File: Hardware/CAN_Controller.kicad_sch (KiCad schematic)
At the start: 21 parts, among them J1 Conn_01x03, J2 Conn_01x08, J3 Conn_01x02, U1 ATtiny814-SS, U2 MCP2515-xSO, U3 MCP2551-I-SN, U4 MCP16331CH, Y1 8 MHz

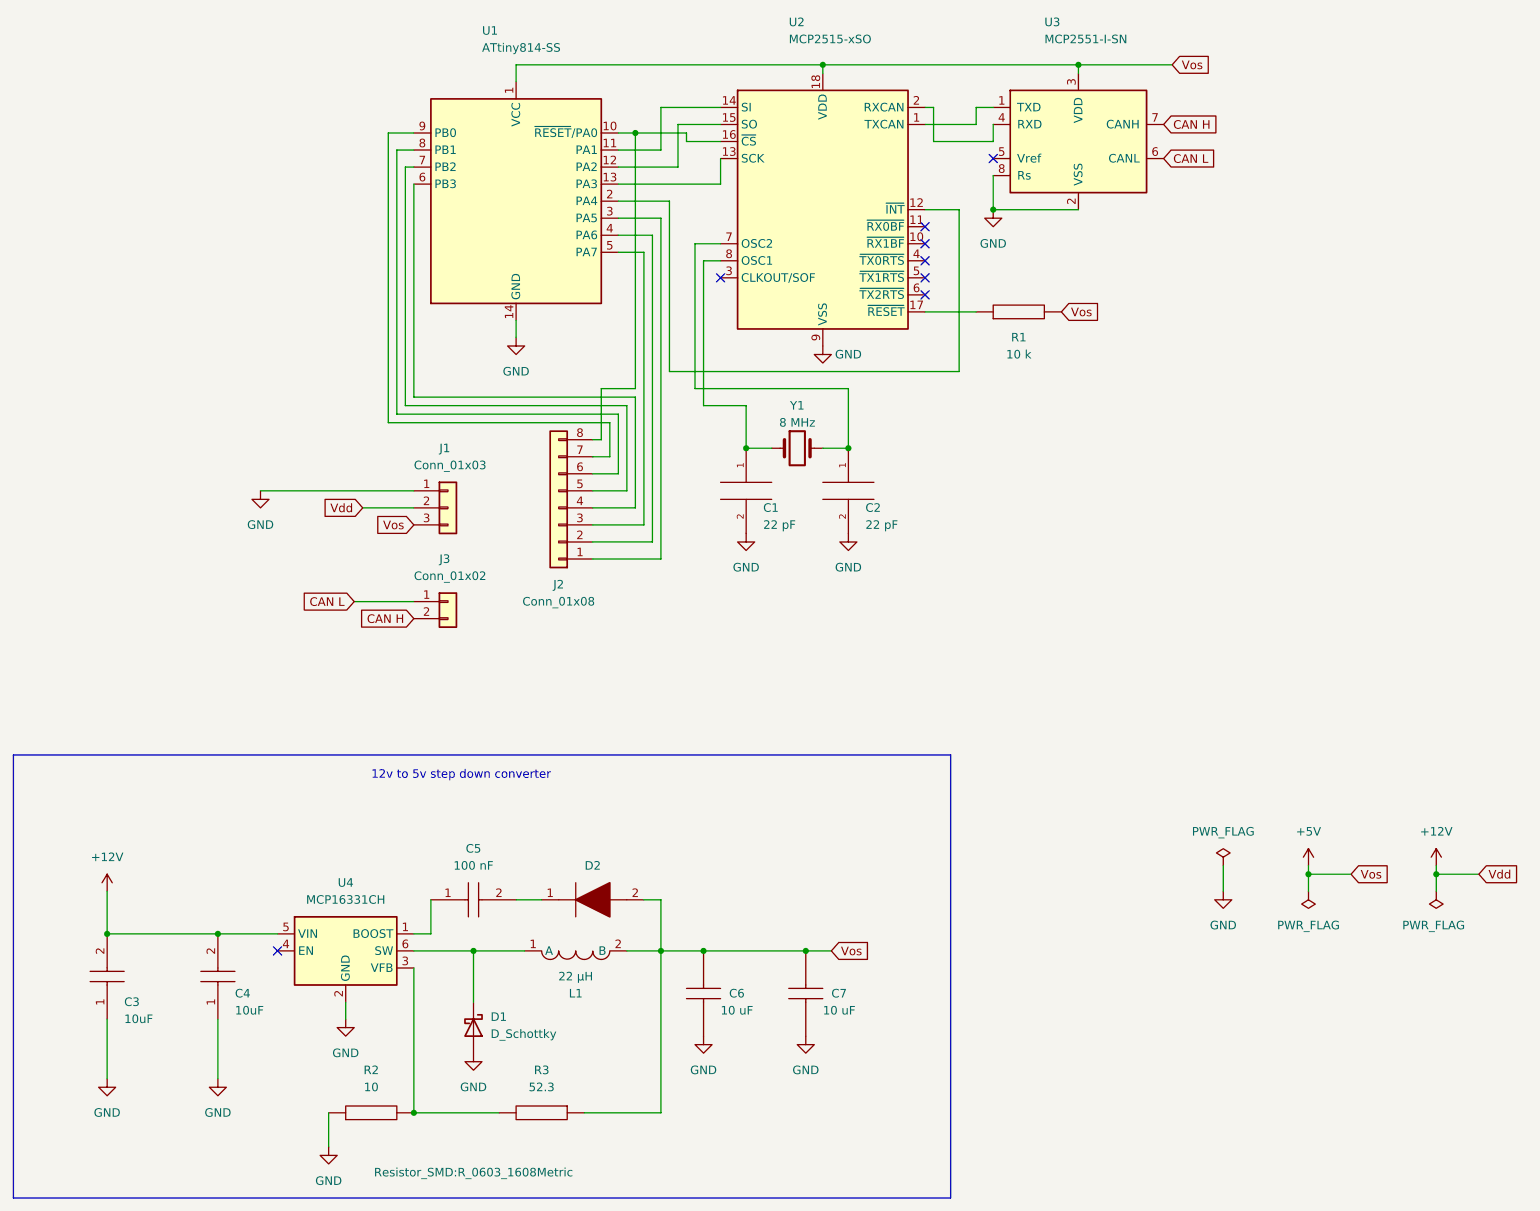
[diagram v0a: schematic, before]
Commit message: rearrainged components to reduce board size and added project footprints
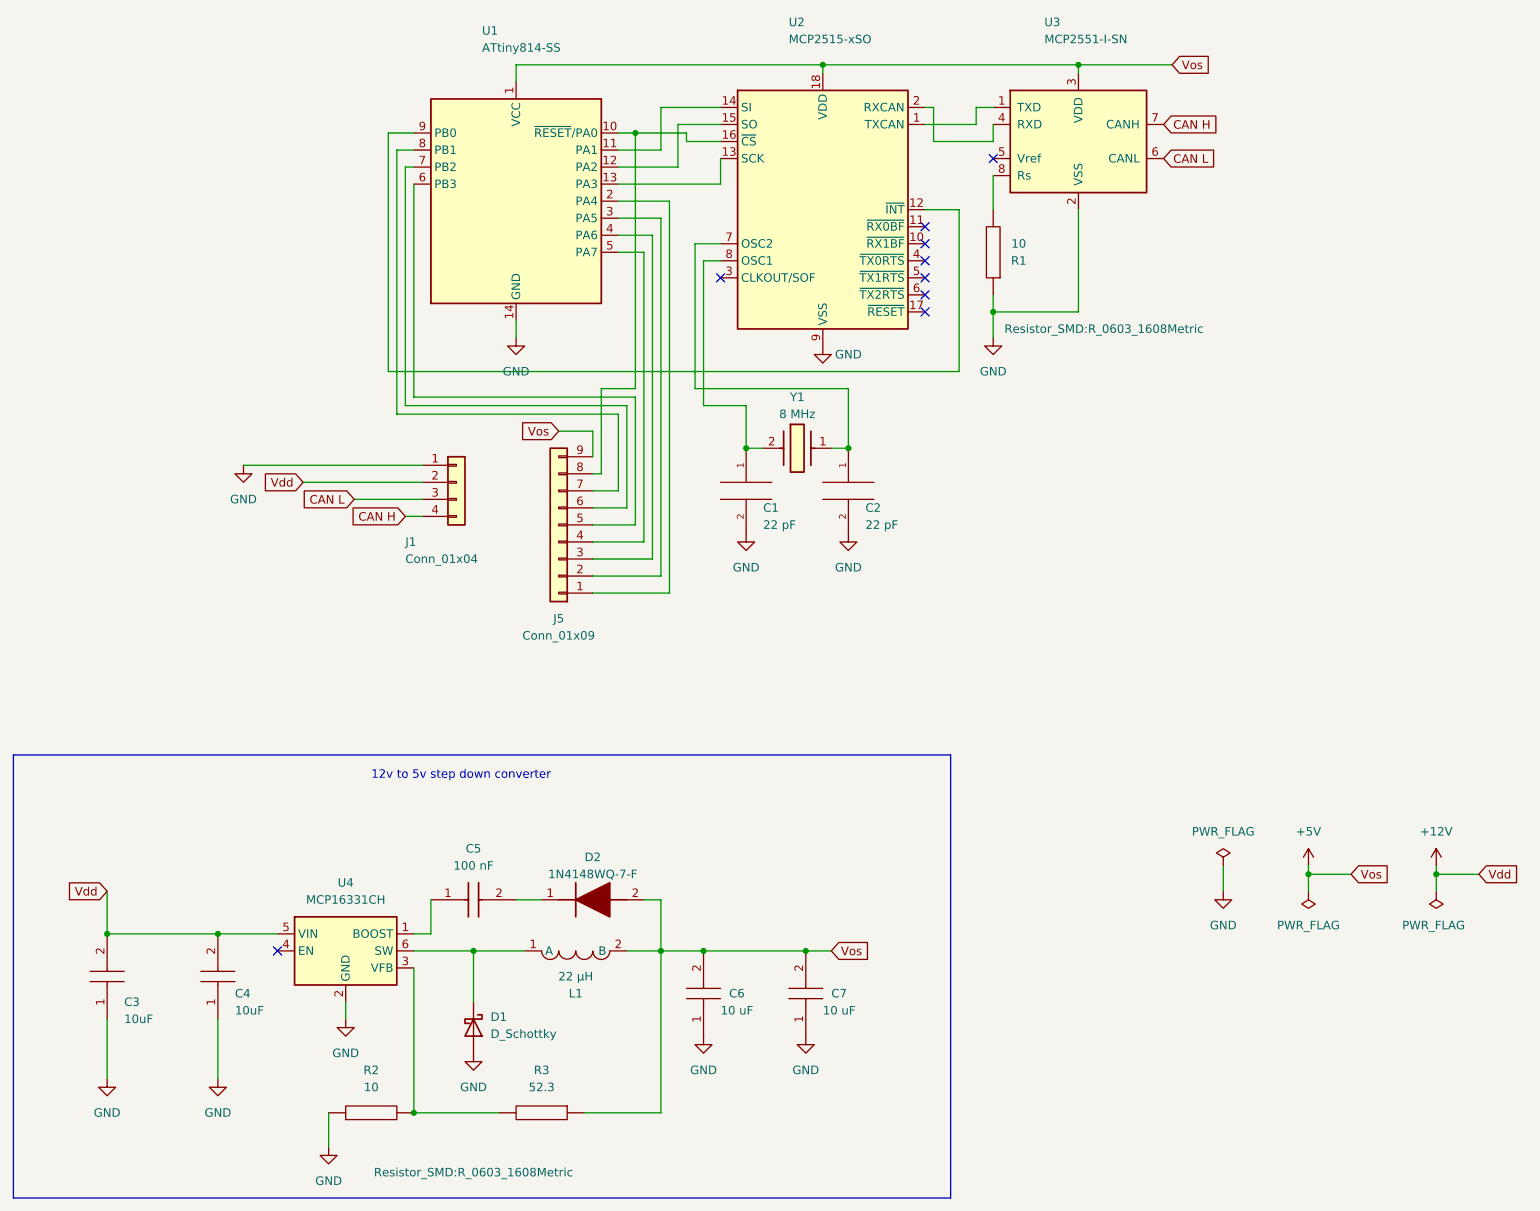
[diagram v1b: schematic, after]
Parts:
- removed D2: 1N4148WQ-7-F, SOD3716X145N, symbol 1N4148_SOD_SMD:1N4148WQ-7-F
- removed J1: Conn_01x03, Connector_PinHeader_2.54mm:PinHeader_1x03_P2.54mm_Vertical, symbol Connector_Generic:Conn_01x03
- removed J2: Conn_01x08, Connector_PinHeader_2.54mm:PinHeader_1x08_P2.54mm_Vertical, symbol Connector_Generic:Conn_01x08
- removed J3: Conn_01x02, Connector_PinHeader_2.54mm:PinHeader_1x02_P2.54mm_Vertical, symbol Connector_Generic:Conn_01x02
- added D2: 1N4148WQ-7-F, SOD3716X145N, symbol 1N4148WQ-7-F:1N4148WQ-7-F
- added J1: Conn_01x04, Connector_PinHeader_2.00mm:PinHeader_1x04_P2.00mm_Vertical, symbol Connector_Generic:Conn_01x04
- added J5: Conn_01x09, Connector_PinHeader_2.00mm:PinHeader_1x09_P2.00mm_Vertical, symbol Connector_Generic:Conn_01x09
- C1, C2: Manufacturer_Part_Number (none) -> C0603C220K3RACAUTO
- C6, C7: footprint C3216_Commercial -> CAPC3216X180N; Height 0.75 -> 1.8
- R1: value 10 k -> 10
- Y1: footprint Crystal:Crystal_SMD_0603-2Pin_6.0x3.5mm -> ECS80830QVSTR; symbol Device:Crystal -> ECS-80-8-30Q-VS-TR:ECS-80-8-30Q-VS-TR; Height (none) -> 1.1; Manufacturer_Name (none) -> ECS; Manufacturer_Part_Number (none) -> ECS-80-8-30Q-VS-TR; Mouser Part Number (none) -> 520-80-8-30Q-VST; Mouser Price/Stock (none) -> https://www.mouser.co.uk/ProductDetail/ECS/ECS-80-8-30Q-VS-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
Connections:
- net +12V: now also J1.2 (Pin_2)
- net +5V: now also D2.2 (A), J5.9 (Pin_9); no longer R1.2
- net CAN H: now also J1.4 (Pin_4)
- net CAN L: now also J1.3 (Pin_3)
- net GND: now also R1.1, J1.1 (Pin_1); no longer U3.8 (Rs)
- net at U2.17 (~{RESET}): no longer R1.1
- net at U1.3 (PA5): now also J5.2 (Pin_2)
- net at U1.4 (PA6): now also J5.3 (Pin_3)
- net at U1.5 (PA7): now also J5.4 (Pin_4)
- net at U1.6 (PB3): now also J5.5 (Pin_5)
- net at U1.7 (PB2): now also J5.6 (Pin_6)
- net at U1.8 (PB1): now also J5.7 (Pin_7)
- net at U1.9 (PB0): now also U2.12 (~{INT})
- net at U1.10 (~{RESET}/PA0), U2.16 (~{CS}): now also J5.8 (Pin_8)
- net at U1.2 (PA4): now also J5.1 (Pin_1); no longer U2.12 (~{INT})
- net at C2.1, U2.7 (OSC2): now also Y1.1 (IN/OUT); no longer Y1.2
- net at C1.1, U2.8 (OSC1): now also Y1.2 (OUT/IN); no longer Y1.1
- net at C5.2: now also D2.1 (K)
- new net: R1.2, U3.8 (Rs)
- no-connect marks 8 -> 9

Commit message: Reduced PCB footprint
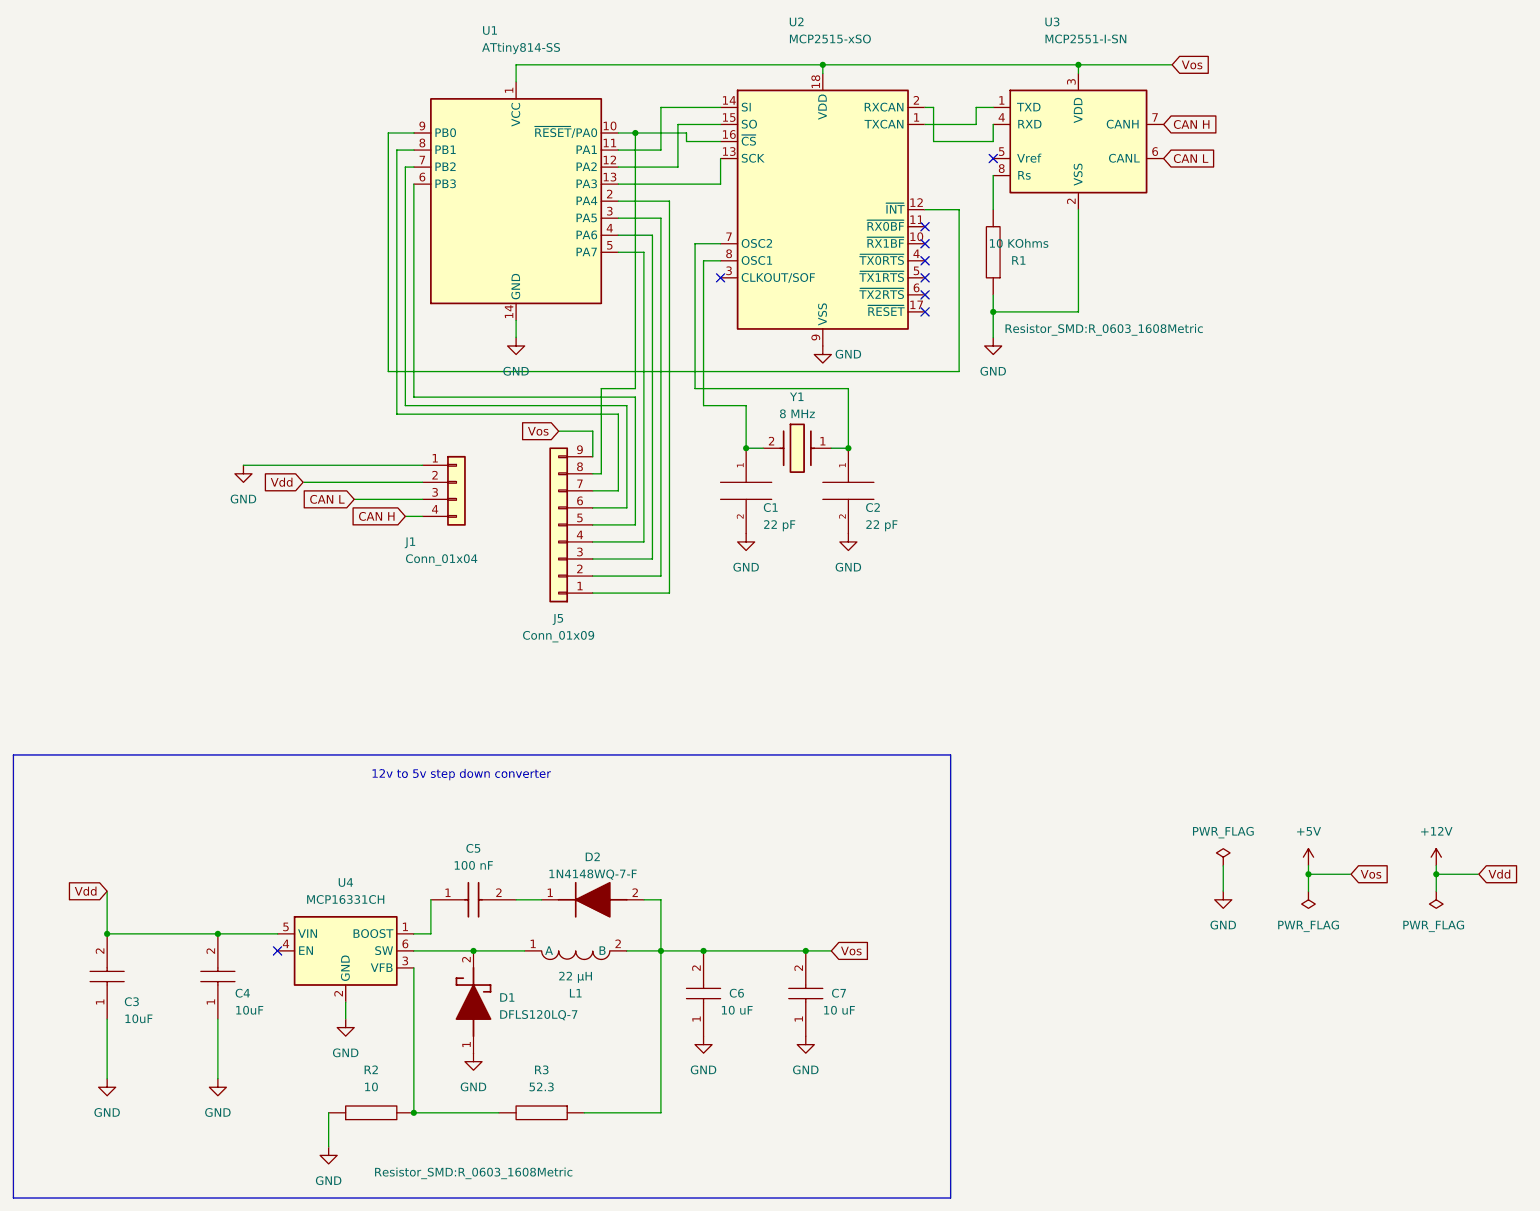
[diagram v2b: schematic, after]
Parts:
- removed D1: D_Schottky, Schottky_Diode:DFLS120L7, symbol Device:D_Schottky
- added D1: DFLS120LQ-7, DFLS120LQ7, symbol DFLS120LQ-7:DFLS120LQ-7
- J1: footprint Connector_PinHeader_2.00mm:PinHeader_1x04_P2.00mm_Vertical -> Connector_PinHeader_2.54mm:PinHeader_1x04_P2.54mm_Vertical
- J5: footprint Connector_PinHeader_2.00mm:PinHeader_1x09_P2.00mm_Vertical -> Connector_PinHeader_2.54mm:PinHeader_1x09_P2.54mm_Vertical
- R1: value 10 -> 10 KOhms
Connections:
- net GND: now also D1.1 (A)
- net at L1.1 (A), U4.6 (SW): now also D1.2 (K)
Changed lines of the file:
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@@
   (junction (at 147.32 24.13) (diameter 0) (color 0 0 0 0)
   )
+  (junction (at 95.25 156.21) (diameter 0) (color 0 0 0 0)
+  )
   (junction (at 219.71 144.78) (diameter 0) (color 0 0 0 0)
-  )
-  (junction (at 95.25 156.21) (diameter 0) (color 0 0 0 0)
   )
   (junction (at 144.78 156.21) (diameter 0) (color 0 0 0 0)
@@
     (stroke (width 0) (type default))
   )
+  (wire (pts (xy 172.72 33.02) (xy 172.72 35.56))
+    (stroke (width 0) (type default))
+  )
+  (wire (pts (xy 185.42 24.13) (xy 199.39 24.13))
+    (stroke (width 0) (type default))
+  )
+  (polyline (pts (xy 26.67 127) (xy 166.37 127))
+    (stroke (width 0) (type default))
+  )
+  (wire (pts (xy 88.9 153.67) (xy 88.9 148.59))
+    (stroke (width 0) (type default))
+  )
+  (polyline (pts (xy 166.37 193.04) (xy 166.37 127))
+    (stroke (width 0) (type default))
+  )
+  (wire (pts (xy 170.18 30.48) (xy 172.72 30.48))
+    (stroke (width 0) (type default))
+  )
+  (wire (pts (xy 107.95 78.74) (xy 113.03 78.74))
+    (stroke (width 0) (type default))
+  )
+  (wire (pts (xy 113.03 97.79) (xy 121.92 97.79))
+    (stroke (width 0) (type default))
+  )
+  (wire (pts (xy 123.19 30.48) (xy 132.08 30.48))
+    (stroke (width 0) (type default))
+  )
+  (wire (pts (xy 123.19 156.21) (xy 123.19 180.34))
+    (stroke (width 0) (type default))
+  )
+  (wire (pts (xy 116.84 49.53) (xy 121.92 49.53))
+    (stroke (width 0) (type default))
+  )
+  (wire (pts (xy 185.42 60.96) (xy 172.72 60.96))
+    (stroke (width 0) (type default))
+  )
+  (wire (pts (xy 86.36 180.34) (xy 86.36 158.75))
+    (stroke (width 0) (type default))
+  )
+  (wire (pts (xy 85.09 39.37) (xy 86.36 39.37))
+    (stroke (width 0) (type default))
+  )
+  (wire (pts (xy 60.96 83.82) (xy 87.63 83.82))
+    (stroke (width 0) (type default))
+  )
+  (wire (pts (xy 82.55 34.29) (xy 86.36 34.29))
+    (stroke (width 0) (type default))
+  )
+  (wire (pts (xy 172.72 60.96) (xy 172.72 64.77))
+    (stroke (width 0) (type default))
+  )
   (wire (pts (xy 95.25 156.21) (xy 102.87 156.21))
     (stroke (width 0) (type default))
   )
-  (wire (pts (xy 172.72 33.02) (xy 172.72 35.56))
-    (stroke (width 0) (type default))
-  )
-  (wire (pts (xy 185.42 24.13) (xy 199.39 24.13))
-    (stroke (width 0) (type default))
-  )
-  (polyline (pts (xy 26.67 127) (xy 166.37 127))
-    (stroke (width 0) (type default))
-  )
-  (wire (pts (xy 88.9 153.67) (xy 88.9 148.59))
-    (stroke (width 0) (type default))
-  )
-  (polyline (pts (xy 166.37 193.04) (xy 166.37 127))
-    (stroke (width 0) (type default))
-  )
-  (wire (pts (xy 170.18 30.48) (xy 172.72 30.48))
-    (stroke (width 0) (type default))
-  )
-  (wire (pts (xy 107.95 78.74) (xy 113.03 78.74))
-    (stroke (width 0) (type default))
-  )
-  (wire (pts (xy 113.03 97.79) (xy 121.92 97.79))
-    (stroke (width 0) (type default))
-  )
-  (wire (pts (xy 123.19 30.48) (xy 132.08 30.48))
-    (stroke (width 0) (type default))
-  )
-  (wire (pts (xy 116.84 49.53) (xy 121.92 49.53))
-    (stroke (width 0) (type default))
-  )
-  (wire (pts (xy 185.42 60.96) (xy 172.72 60.96))
-    (stroke (width 0) (type default))
-  )
-  (wire (pts (xy 86.36 180.34) (xy 86.36 158.75))
-    (stroke (width 0) (type default))
-  )
-  (wire (pts (xy 85.09 39.37) (xy 86.36 39.37))
-    (stroke (width 0) (type default))
-  )
-  (wire (pts (xy 60.96 83.82) (xy 87.63 83.82))
-    (stroke (width 0) (type default))
-  )
-  (wire (pts (xy 82.55 34.29) (xy 86.36 34.29))
-    (stroke (width 0) (type default))
-  )
-  (wire (pts (xy 172.72 60.96) (xy 172.72 64.77))
-    (stroke (width 0) (type default))
-  )
   (wire (pts (xy 83.82 76.2) (xy 116.84 76.2))
     (stroke (width 0) (type default))
@@
     (stroke (width 0) (type default))
   )
-  (wire (pts (xy 123.19 156.21) (xy 123.19 180.34))
-    (stroke (width 0) (type default))
-  )
   (wire (pts (xy 129.54 74.93) (xy 135.89 74.93))
     (stroke (width 0) (type default))
@@
   )
   (wire (pts (xy 119.38 34.29) (xy 127 34.29))
-    (stroke (width 0) (type default))
-  )
-  (wire (pts (xy 95.25 156.21) (xy 95.25 163.83))
     (stroke (width 0) (type default))
   )
@@
       (effects (font (size 1.27 1.27)))
     )
-    (property "Value" "10" (at 176.53 50.8 0)
+    (property "Value" "10 KOhms" (at 176.53 50.8 0)
       (effects (font (size 1.27 1.27)))
     )
@@
     )
   )
+  (symbol (lib_id "DFLS120LQ-7:DFLS120LQ-7") (at 95.25 153.67 270) (unit 1)
+    (in_bom yes) (on_board yes) (dnp no) (fields_autoplaced)
+    (property "Reference" "D1" (at 99.06 163.195 90)
+      (effects (font (size 1.27 1.27)) (justify left))
+    )
+    (property "Value" "DFLS120LQ-7" (at 99.06 165.735 90)
+      (effects (font (size 1.27 1.27)) (justify left))
+    )
+    (property "Footprint" "DFLS120LQ7" (at 1.6 166.37 0)
+      (effects (font (size 1.27 1.27)) (justify left top) hide)
+    )
+    (property "Datasheet" "https://componentsearchengine.com/Datasheets/1/DFLS120LQ-7.pdf" (at -98.4 166.37 0)
+      (effects (font (size 1.27 1.27)) (justify left top) hide)
+    )
+    (property "Height" "" (at -298.4 166.37 0)
+      (effects (font (size 1.27 1.27)) (justify left top) hide)
+    )
+    (property "Mouser Part Number" "621-DFLS120LQ7" (at -398.4 166.37 0)
+      (effects (font (size 1.27 1.27)) (justify left top) hide)
+    )
+    (property "Mouser Price/Stock" "https://www.mouser.com/Search/Refine.aspx?Keyword=621-DFLS120LQ7" (at -498.4 166.37 0)
+      (effects (font (size 1.27 1.27)) (justify left top) hide)
+    )
+    (property "Manufacturer_Name" "Diodes Inc." (at -598.4 166.37 0)
+      (effects (font (size 1.27 1.27)) (justify left top) hide)
+    )
+    (property "Manufacturer_Part_Number" "DFLS120LQ-7" (at -698.4 166.37 0)
+      (effects (font (size 1.27 1.27)) (justify left top) hide)
+    )
+    (pin "1")
+    (pin "2")
+    (instances
+      (project "CAN_Controller"
+        (path "/cd098e14-1fbf-4252-bea9-fb7f332659be"
+          (reference "D1") (unit 1)
+        )
+      )
+    )
+  )
   (symbol (lib_id "power:GND") (at 147.32 66.04 0) (unit 1)
     (in_bom yes) (on_board yes) (dnp no)
@@
       (effects (font (size 1.27 1.27)))
     )
-    (property "Footprint" "Connector_PinHeader_2.00mm:PinHeader_1x09_P2.00mm_Vertical" (at 107.95 92.71 0)
+    (property "Footprint" "Connector_PinHeader_2.54mm:PinHeader_1x09_P2.54mm_Vertical" (at 107.95 92.71 0)
       (effects (font (size 1.27 1.27)) hide)
     )
@@
     )
   )
-  (symbol (lib_id "Device:D_Schottky") (at 95.25 167.64 270) (unit 1)
-    (in_bom yes) (on_board yes) (dnp no) (fields_autoplaced)
-    (property "Reference" "D1" (at 97.79 166.0524 90)
-      (effects (font (size 1.27 1.27)) (justify left))
-    )
-    (property "Value" "D_Schottky" (at 97.79 168.5924 90)
-      (effects (font (size 1.27 1.27)) (justify left))
-    )
-    (property "Footprint" "Schottky_Diode:DFLS120L7" (at 95.25 167.64 0)
-      (effects (font (size 1.27 1.27)) hide)
-    )
-    (property "Datasheet" "~" (at 95.25 167.64 0)
-      (effects (font (size 1.27 1.27)) hide)
-    )
-    (pin "1")
-    (pin "2")
-    (instances
-      (project "CAN_Controller"
-        (path "/cd098e14-1fbf-4252-bea9-fb7f332659be"
-          (reference "D1") (unit 1)
-        )
-      )
-    )
-  )
   (symbol (lib_id "1N4148WQ-7-F:1N4148WQ-7-F") (at 105.41 148.59 0) (unit 1)
     (in_bom yes) (on_board yes) (dnp no) (fields_autoplaced)
@@
       (effects (font (size 1.27 1.27)) (justify left))
     )
-    (property "Footprint" "Connector_PinHeader_2.00mm:PinHeader_1x04_P2.00mm_Vertical" (at 99.06 102.87 0)
-      (effects (font (size 1.27 1.27)) hide)
-    )
+    (property "Footprint" "Connector_PinHeader_2.54mm:PinHeader_1x04_P2.54mm_Vertical" (at 99.06 102.87 0)
+      (effects (font (size 1.27 1.27)) hide)
+    )
